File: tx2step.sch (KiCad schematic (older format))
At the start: 57 parts, among them CON1 BARREL_JACK, IC1 TPS2113A, IC3 MCP73831, IC4 TPS61202, IC5 DRV8834, IC6 DRV8834, J1 8P8C, J2 6P4Cx2, J4 Prog, J5 CHASSIS_SWITCHES, SW1 SW_DIP_x02, U1 ATmega328P-MMH, Y1 16 MHz

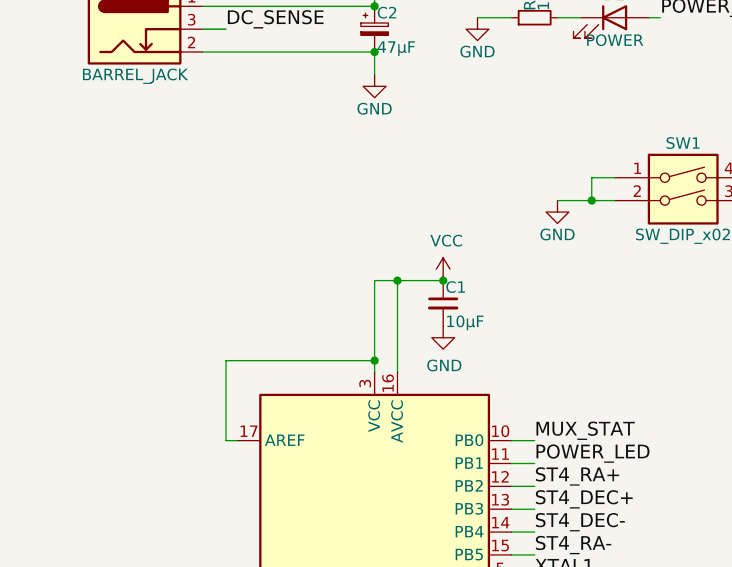
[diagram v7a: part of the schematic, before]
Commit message: Add separate bypass capacitors for AVR VCC/AVCC
They're on opposite sides of the chip and should probably each
have their own bypass
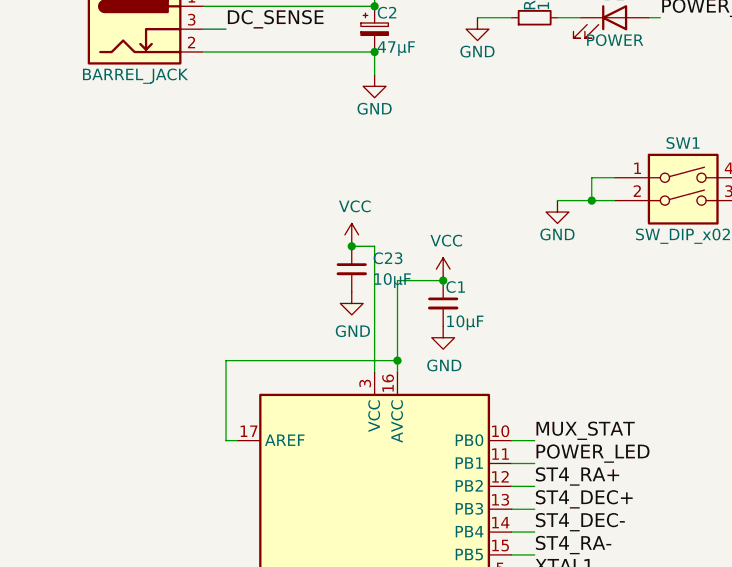
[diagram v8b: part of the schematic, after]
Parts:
- added C23: 10µF, Capacitor_SMD:C_0603_1608Metric, symbol Device:C_Small
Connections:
- net GND: now also C23.2
- net VCC: now also C23.1
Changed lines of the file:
@@
 $EndComp
 Wire Wire Line
-	2000 2150 2000 2500
-Wire Wire Line
-	2100 2150 2100 2550
+	2100 2150 2100 2500
 $Comp
 L power:GND #PWR06
@@
 	1350 2850 1350 2500
 Wire Wire Line
-	1350 2500 2000 2500
-Wire Wire Line
 	1350 2850 1400 2850
-Connection ~ 2000 2500
-Wire Wire Line
-	2000 2500 2000 2550
 Wire Wire Line
 	2600 2850 2700 2850
@@
 	5050 4800 5550 4800
 Wire Wire Line
-	2000 2150 2100 2150
-Connection ~ 2100 2150
-Wire Wire Line
 	2100 2150 2300 2150
 Wire Wire Line
@@
 	4800 1700 4800 1750
 Connection ~ 4350 2150
+Wire Wire Line
+	1350 2500 2100 2500
+Connection ~ 2100 2500
+Wire Wire Line
+	2100 2500 2100 2550
+Wire Wire Line
+	2000 2550 2000 2000
+Wire Wire Line
+	2000 2000 1900 2000
+$Comp
+L Device:C_Small C23
+U 1 1 5FD2AE45
+P 1900 2100
+F 0 "C23" H 1992 2146 50  0000 L CNN
+F 1 "10µF" H 1992 2055 50  0000 L CNN
+F 2 "Capacitor_SMD:C_0603_1608Metric" H 1900 2100 50  0001 C CNN
+F 3 "~" H 1900 2100 50  0001 C CNN
+	1    1900 2100
+	1    0    0    -1
+$EndComp
+$Comp
+L power:VCC #PWR047
+U 1 1 5FD2CD50
+P 1900 2000
+F 0 "#PWR047" H 1900 1850 50  0001 C CNN
+F 1 "VCC" H 1915 2173 50  0000 C CNN
+F 2 "" H 1900 2000 50  0001 C CNN
+F 3 "" H 1900 2000 50  0001 C CNN
+	1    1900 2000
+	1    0    0    -1
+$EndComp
+$Comp
+L power:GND #PWR048
+U 1 1 5FD2DD4E
+P 1900 2200
+F 0 "#PWR048" H 1900 1950 50  0001 C CNN
+F 1 "GND" H 1905 2027 50  0000 C CNN
+F 2 "" H 1900 2200 50  0001 C CNN
+F 3 "" H 1900 2200 50  0001 C CNN
+	1    1900 2200
+	1    0    0    -1
+$EndComp
+Connection ~ 1900 2000
 $EndSCHEMATC
